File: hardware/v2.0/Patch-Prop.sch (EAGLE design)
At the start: 49 parts, among them IC1 TPS77033, IC2 XBEE, IC3 MMA8452Q, IC4 ATMEGA168, IC5 MCP1253, IC6 W2RV005RM, U2 MCP73831, X1 USBSMD

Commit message: Cleanup
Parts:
- added R10: 4.7k, rcl:R-US_R0603
- added R6: RLim, rcl:R-US_R0603
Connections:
- new net N$12: IC6.IN3, R9.1
- new net N$4: R6.2, T2.E
- new net N$7: IC6.IN1, R8.1
- new net N$9: IC6.IN2, R10.1
- net +3V3: no longer R8.2, R9.2
- net BLUE: now also R8.2; no longer IC6.IN1
- net GND: now also R6.1; no longer T2.E
- net GREEN: now also R10.2; no longer IC6.IN2
- net RED: now also R9.2; no longer IC6.IN3
- net SCL: no longer R9.1
- net SDA: no longer R8.1
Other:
- moved on the sheet: JP6, R8, R9, T2
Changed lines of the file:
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@@
 <part name="GND13" library="supply1" deviceset="GND" device=""/>
 <part name="SJ3" library="SparkFun" deviceset="SOLDERJUMPER" device="NO"/>
+<part name="R6" library="rcl" deviceset="R-US_" device="R0603" value="RLim"/>
 <part name="R8" library="rcl" deviceset="R-US_" device="R0603" value="4.7k"/>
 <part name="R9" library="rcl" deviceset="R-US_" device="R0603" value="4.7k"/>
-<part name="+3V14" library="supply1" deviceset="+3V3" device=""/>
-<part name="+3V15" library="supply1" deviceset="+3V3" device=""/>
+<part name="R10" library="rcl" deviceset="R-US_" device="R0603" value="4.7k"/>
 </parts>
 <sheets>
@@
 <instance part="SJ1" gate="1" x="424.18" y="350.52" rot="R180"/>
 <instance part="T1" gate="G$1" x="505.46" y="335.28" rot="R270"/>
-<instance part="T2" gate="G$1" x="86.36" y="104.14"/>
+<instance part="T2" gate="G$1" x="86.36" y="96.52"/>
 <instance part="GND11" gate="1" x="218.44" y="337.82"/>
 <instance part="LED1" gate="G$1" x="259.08" y="210.82"/>
@@
 <instance part="GND12" gate="1" x="259.08" y="200.66"/>
 <instance part="+3V10" gate="G$1" x="259.08" y="228.6"/>
-<instance part="GND10" gate="1" x="88.9" y="93.98"/>
+<instance part="GND10" gate="1" x="88.9" y="73.66"/>
 <instance part="U2" gate="G$1" x="114.3" y="335.28"/>
 <instance part="GND17" gate="1" x="101.6" y="312.42"/>
@@
 <instance part="P+3" gate="1" x="355.6" y="370.84"/>
 <instance part="+3V13" gate="G$1" x="269.24" y="370.84"/>
-<instance part="JP6" gate="G$1" x="78.74" y="71.12" rot="MR180"/>
-<instance part="SUPPLY6" gate="1" x="88.9" y="76.2"/>
+<instance part="JP6" gate="G$1" x="78.74" y="43.18" rot="MR180"/>
+<instance part="SUPPLY6" gate="1" x="88.9" y="48.26"/>
 <instance part="PROPINQUITY_V2" gate="G$1" x="0" y="0"/>
 <instance part="PROPINQUITY_V2" gate="G$2" x="452.12" y="0"/>
@@
 <instance part="GND13" gate="1" x="538.48" y="81.28"/>
 <instance part="SJ3" gate="1" x="213.36" y="231.14" rot="R180"/>
-<instance part="R8" gate="G$1" x="408.94" y="233.68" rot="R90"/>
-<instance part="R9" gate="G$1" x="401.32" y="233.68" rot="R90"/>
-<instance part="+3V14" gate="G$1" x="408.94" y="243.84"/>
-<instance part="+3V15" gate="G$1" x="401.32" y="243.84"/>
+<instance part="R6" gate="G$1" x="88.9" y="83.82" rot="R90"/>
+<instance part="R8" gate="G$1" x="467.36" y="99.06" rot="R180"/>
+<instance part="R9" gate="G$1" x="467.36" y="88.9" rot="R180"/>
+<instance part="R10" gate="G$1" x="467.36" y="93.98" rot="R180"/>
 </instances>
 <busses>
@@
 <wire x1="426.72" y1="335.28" x2="426.72" y2="337.82" width="0.1524" layer="91"/>
 <wire x1="426.72" y1="337.82" x2="431.8" y2="337.82" width="0.1524" layer="91"/>
-</segment>
-<segment>
-<pinref part="T2" gate="G$1" pin="E"/>
-<wire x1="88.9" y1="99.06" x2="88.9" y2="96.52" width="0.1524" layer="91"/>
-<pinref part="GND10" gate="1" pin="GND"/>
 </segment>
 <segment>
@@
 <wire x1="223.52" y1="195.58" x2="223.52" y2="193.04" width="0.1524" layer="91"/>
 </segment>
+<segment>
+<pinref part="R6" gate="G$1" pin="1"/>
+<pinref part="GND10" gate="1" pin="GND"/>
+<wire x1="88.9" y1="78.74" x2="88.9" y2="76.2" width="0.1524" layer="91"/>
+</segment>
 </net>
 <net name="+3V3" class="0">
@@
 </segment>
 <segment>
-<pinref part="+3V15" gate="G$1" pin="+3V3"/>
-<pinref part="R9" gate="G$1" pin="2"/>
-<wire x1="401.32" y1="241.3" x2="401.32" y2="238.76" width="0.1524" layer="91"/>
-</segment>
-<segment>
-<pinref part="+3V14" gate="G$1" pin="+3V3"/>
-<pinref part="R8" gate="G$1" pin="2"/>
-<wire x1="408.94" y1="241.3" x2="408.94" y2="238.76" width="0.1524" layer="91"/>
-</segment>
-<segment>
 <pinref part="ISP1" gate="A" pin="2"/>
 <pinref part="+3V7" gate="G$1" pin="+3V3"/>
@@
 <segment>
 <pinref part="SUPPLY6" gate="1" pin="V+"/>
-<wire x1="88.9" y1="71.12" x2="88.9" y2="73.66" width="0.1524" layer="91"/>
+<wire x1="88.9" y1="43.18" x2="88.9" y2="45.72" width="0.1524" layer="91"/>
 <pinref part="JP6" gate="G$1" pin="1"/>
-<wire x1="88.9" y1="71.12" x2="86.36" y2="71.12" width="0.1524" layer="91"/>
+<wire x1="88.9" y1="43.18" x2="86.36" y2="43.18" width="0.1524" layer="91"/>
 </segment>
 <segment>
@@
 <net name="RED" class="0">
 <segment>
-<pinref part="IC6" gate="G$1" pin="IN3"/>
-<wire x1="464.82" y1="88.9" x2="474.98" y2="88.9" width="0.1524" layer="91"/>
-<label x="464.82" y="88.9" size="1.27" layer="95" font="vector" ratio="15" rot="R180" xref="yes"/>
+<wire x1="459.74" y1="88.9" x2="462.28" y2="88.9" width="0.1524" layer="91"/>
+<label x="459.74" y="88.9" size="1.27" layer="95" font="vector" ratio="15" rot="R180" xref="yes"/>
+<pinref part="R9" gate="G$1" pin="2"/>
 </segment>
 <segment>
@@
 </segment>
 <segment>
-<pinref part="IC6" gate="G$1" pin="IN1"/>
-<wire x1="474.98" y1="99.06" x2="464.82" y2="99.06" width="0.1524" layer="91"/>
-<label x="464.82" y="99.06" size="1.27" layer="95" font="vector" ratio="15" rot="R180" xref="yes"/>
+<label x="459.74" y="99.06" size="1.27" layer="95" font="vector" ratio="15" rot="R180" xref="yes"/>
+<pinref part="R8" gate="G$1" pin="2"/>
+<wire x1="462.28" y1="99.06" x2="459.74" y2="99.06" width="0.1524" layer="91"/>
 </segment>
 </net>
@@
 <segment>
 <pinref part="T2" gate="G$1" pin="B"/>
-<wire x1="83.82" y1="104.14" x2="81.28" y2="104.14" width="0.1524" layer="91"/>
-<label x="81.28" y="104.14" size="1.27" layer="95" font="vector" ratio="15" rot="R180" xref="yes"/>
+<wire x1="83.82" y1="96.52" x2="81.28" y2="96.52" width="0.1524" layer="91"/>
+<label x="81.28" y="96.52" size="1.27" layer="95" font="vector" ratio="15" rot="R180" xref="yes"/>
 </segment>
 <segment>
@@
 <segment>
 <pinref part="T2" gate="G$1" pin="C"/>
-<wire x1="88.9" y1="109.22" x2="88.9" y2="111.76" width="0.1524" layer="91"/>
-<label x="88.9" y="111.76" size="1.27" layer="95" font="vector" ratio="15" rot="R90" xref="yes"/>
+<wire x1="88.9" y1="101.6" x2="88.9" y2="104.14" width="0.1524" layer="91"/>
+<label x="88.9" y="104.14" size="1.27" layer="95" font="vector" ratio="15" rot="R90" xref="yes"/>
 </segment>
 <segment>
 <pinref part="JP6" gate="G$1" pin="2"/>
-<wire x1="86.36" y1="68.58" x2="91.44" y2="68.58" width="0.1524" layer="91"/>
-<label x="91.44" y="68.58" size="1.27" layer="95" font="vector" ratio="15" xref="yes"/>
+<wire x1="86.36" y1="40.64" x2="91.44" y2="40.64" width="0.1524" layer="91"/>
+<label x="91.44" y="40.64" size="1.27" layer="95" font="vector" ratio="15" xref="yes"/>
 </segment>
 </net>
@@
 <net name="SCL" class="0">
 <segment>
-<wire x1="441.96" y1="220.98" x2="401.32" y2="220.98" width="0.1524" layer="91"/>
+<wire x1="441.96" y1="220.98" x2="393.7" y2="220.98" width="0.1524" layer="91"/>
 <label x="393.7" y="220.98" size="1.27" layer="95" font="vector" ratio="15" rot="R180" xref="yes"/>
 <pinref part="IC3" gate="G$1" pin="SCL"/>
-<pinref part="R9" gate="G$1" pin="1"/>
-<wire x1="401.32" y1="220.98" x2="393.7" y2="220.98" width="0.1524" layer="91"/>
-<wire x1="401.32" y1="228.6" x2="401.32" y2="220.98" width="0.1524" layer="91"/>
-<junction x="401.32" y="220.98"/>
 </segment>
 <segment>
@@
 <net name="SDA" class="0">
 <segment>
-<wire x1="441.96" y1="223.52" x2="408.94" y2="223.52" width="0.1524" layer="91"/>
+<wire x1="441.96" y1="223.52" x2="393.7" y2="223.52" width="0.1524" layer="91"/>
 <label x="393.7" y="223.52" size="1.27" layer="95" font="vector" ratio="15" rot="R180" xref="yes"/>
 <pinref part="IC3" gate="G$1" pin="SDA"/>
-<pinref part="R8" gate="G$1" pin="1"/>
-<wire x1="408.94" y1="223.52" x2="393.7" y2="223.52" width="0.1524" layer="91"/>
-<wire x1="408.94" y1="228.6" x2="408.94" y2="223.52" width="0.1524" layer="91"/>
-<junction x="408.94" y="223.52"/>
 </segment>
 <segment>
@@
 <net name="GREEN" class="0">
 <segment>
-<pinref part="IC6" gate="G$1" pin="IN2"/>
-<wire x1="474.98" y1="93.98" x2="464.82" y2="93.98" width="0.1524" layer="91"/>
-<label x="464.82" y="93.98" size="1.27" layer="95" font="vector" ratio="15" rot="R180" xref="yes"/>
+<label x="459.74" y="93.98" size="1.27" layer="95" font="vector" ratio="15" rot="R180" xref="yes"/>
+<pinref part="R10" gate="G$1" pin="2"/>
+<wire x1="459.74" y1="93.98" x2="462.28" y2="93.98" width="0.1524" layer="91"/>
 </segment>
 <segment>
@@
 </segment>
 </net>
+<net name="N$4" class="0">
+<segment>
+<pinref part="T2" gate="G$1" pin="E"/>
+<pinref part="R6" gate="G$1" pin="2"/>
+<wire x1="88.9" y1="91.44" x2="88.9" y2="88.9" width="0.1524" layer="91"/>
+</segment>
+</net>
+<net name="N$7" class="0">
+<segment>
+<pinref part="R8" gate="G$1" pin="1"/>
+<pinref part="IC6" gate="G$1" pin="IN1"/>
+<wire x1="472.44" y1="99.06" x2="474.98" y2="99.06" width="0.1524" layer="91"/>
+</segment>
+</net>
+<net name="N$9" class="0">
+<segment>
+<pinref part="R10" gate="G$1" pin="1"/>
+<pinref part="IC6" gate="G$1" pin="IN2"/>
+<wire x1="472.44" y1="93.98" x2="474.98" y2="93.98" width="0.1524" layer="91"/>
+</segment>
+</net>
+<net name="N$12" class="0">
+<segment>
+<pinref part="IC6" gate="G$1" pin="IN3"/>
+<pinref part="R9" gate="G$1" pin="1"/>
+<wire x1="474.98" y1="88.9" x2="472.44" y2="88.9" width="0.1524" layer="91"/>
+</segment>
+</net>

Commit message: Moved uC now routing LEDs
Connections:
- net GREEN: now also IC4.PD5(T1), R9.2; no longer IC4.PB1(OC1A), R10.2
- net GREEN_OUT: now also IC6.OUT3; no longer IC6.OUT2
- net RED: now also IC4.PB1(OC1A), R10.2; no longer IC4.PD5(T1), R9.2
- net RED_OUT: now also IC6.OUT2; no longer IC6.OUT3
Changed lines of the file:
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@@
 </segment>
 </net>
-<net name="RED" class="0">
+<net name="GREEN" class="0">
 <segment>
 <wire x1="459.74" y1="88.9" x2="462.28" y2="88.9" width="0.1524" layer="91"/>
@@
 </segment>
 </net>
-<net name="GREEN" class="0">
+<net name="RED" class="0">
 <segment>
 <label x="459.74" y="93.98" size="1.27" layer="95" font="vector" ratio="15" rot="R180" xref="yes"/>
@@
 </segment>
 <segment>
+<pinref part="IC6" gate="G$1" pin="OUT3"/>
+<wire x1="518.16" y1="83.82" x2="510.54" y2="83.82" width="0.1524" layer="91"/>
+<label x="518.16" y="83.82" size="1.27" layer="95" font="vector" ratio="15" xref="yes"/>
+</segment>
+</net>
+<net name="RED_OUT" class="0">
+<segment>
+<pinref part="LED3" gate="G$1" pin="RED_C"/>
+<wire x1="416.56" y1="111.76" x2="424.18" y2="111.76" width="0.1524" layer="91"/>
+<label x="424.18" y="111.76" size="1.27" layer="95" font="vector" ratio="15" xref="yes"/>
+</segment>
+<segment>
+<pinref part="LED4" gate="G$1" pin="RED_C"/>
+<wire x1="424.18" y1="86.36" x2="416.56" y2="86.36" width="0.1524" layer="91"/>
+<label x="424.18" y="86.36" size="1.27" layer="95" font="vector" ratio="15" xref="yes"/>
+</segment>
+<segment>
+<pinref part="LED5" gate="G$1" pin="RED_C"/>
+<wire x1="424.18" y1="63.5" x2="416.56" y2="63.5" width="0.1524" layer="91"/>
+<label x="424.18" y="63.5" size="1.27" layer="95" font="vector" ratio="15" xref="yes"/>
+</segment>
+<segment>
+<pinref part="LED6" gate="G$1" pin="RED_C"/>
+<wire x1="424.18" y1="40.64" x2="416.56" y2="40.64" width="0.1524" layer="91"/>
+<label x="424.18" y="40.64" size="1.27" layer="95" font="vector" ratio="15" xref="yes"/>
+</segment>
+<segment>
 <pinref part="IC6" gate="G$1" pin="OUT2"/>
 <wire x1="510.54" y1="88.9" x2="518.16" y2="88.9" width="0.1524" layer="91"/>
@@
 </segment>
 </net>
-<net name="RED_OUT" class="0">
-<segment>
-<pinref part="LED3" gate="G$1" pin="RED_C"/>
-<wire x1="416.56" y1="111.76" x2="424.18" y2="111.76" width="0.1524" layer="91"/>
-<label x="424.18" y="111.76" size="1.27" layer="95" font="vector" ratio="15" xref="yes"/>
-</segment>
-<segment>
-<pinref part="LED4" gate="G$1" pin="RED_C"/>
-<wire x1="424.18" y1="86.36" x2="416.56" y2="86.36" width="0.1524" layer="91"/>
-<label x="424.18" y="86.36" size="1.27" layer="95" font="vector" ratio="15" xref="yes"/>
-</segment>
-<segment>
-<pinref part="LED5" gate="G$1" pin="RED_C"/>
-<wire x1="424.18" y1="63.5" x2="416.56" y2="63.5" width="0.1524" layer="91"/>
-<label x="424.18" y="63.5" size="1.27" layer="95" font="vector" ratio="15" xref="yes"/>
-</segment>
-<segment>
-<pinref part="LED6" gate="G$1" pin="RED_C"/>
-<wire x1="424.18" y1="40.64" x2="416.56" y2="40.64" width="0.1524" layer="91"/>
-<label x="424.18" y="40.64" size="1.27" layer="95" font="vector" ratio="15" xref="yes"/>
-</segment>
-<segment>
-<pinref part="IC6" gate="G$1" pin="OUT3"/>
-<wire x1="518.16" y1="83.82" x2="510.54" y2="83.82" width="0.1524" layer="91"/>
-<label x="518.16" y="83.82" size="1.27" layer="95" font="vector" ratio="15" xref="yes"/>
-</segment>
-</net>

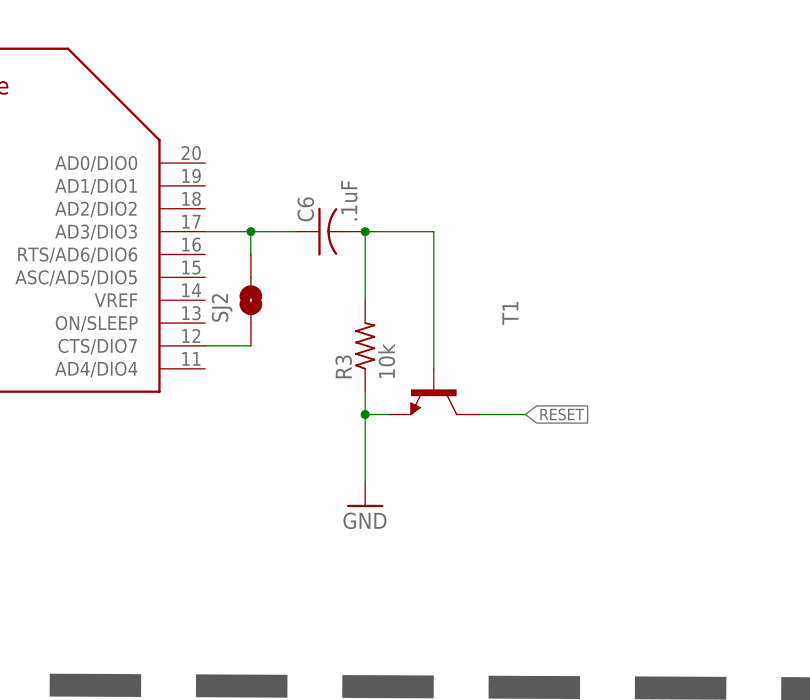
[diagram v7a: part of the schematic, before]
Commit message: Working on LED routing, remove Xbee reset
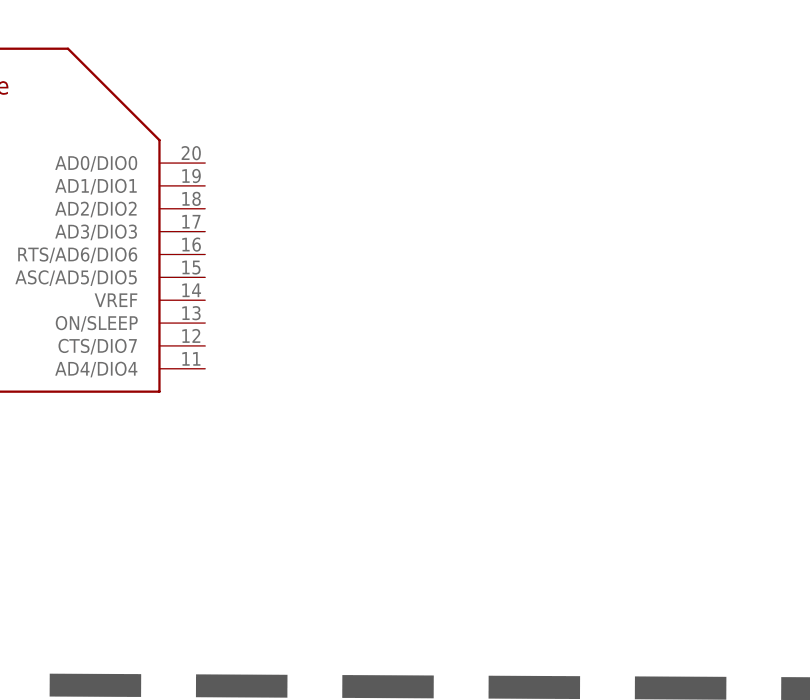
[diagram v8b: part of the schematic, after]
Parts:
- removed C6: .1uF, rcl:C-USC0603
- removed R3: 10k, rcl:R-US_R0603
- removed SJ2: SOLDERJUMPERNO, SparkFun:SOLDERJUMPERNO
- removed T1: (no value), transistor:-NPN-SOT23-EBC
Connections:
- removed net N$1: C6.1, IC2.AD3/DIO3, SJ2.2
- removed net N$18: IC2.CTS/DIO7, SJ2.1
- removed net N$2: C6.2, R3.2, T1.B
- net GND: no longer R3.1, T1.E
- net RESET: no longer T1.C
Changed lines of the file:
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@@
 <part name="C2" library="rcl" deviceset="C-US" device="C0603" value="4.7uF"/>
 <part name="C3" library="rcl" deviceset="C-US" device="C0603" value="1uF"/>
-<part name="R3" library="rcl" deviceset="R-US_" device="R0603" value="10k"/>
 <part name="+3V3" library="supply1" deviceset="+3V3" device=""/>
 <part name="SUPPLY1" library="supply2" deviceset="V+" device=""/>
@@
 <part name="+3V2" library="supply1" deviceset="+3V3" device=""/>
 <part name="GND1" library="supply1" deviceset="GND" device=""/>
-<part name="C6" library="rcl" deviceset="C-US" device="C0603" value=".1uF"/>
-<part name="GND2" library="supply1" deviceset="GND" device=""/>
 <part name="IC4" library="SparkFun" deviceset="ATMEGA168" device=""/>
 <part name="C13" library="rcl" deviceset="C-US" device="C0603" value="10uF"/>
@@
 <part name="LED5" library="adafruit" deviceset="RGBLED" device="5050"/>
 <part name="LED6" library="adafruit" deviceset="RGBLED" device="5050"/>
-<part name="SJ2" library="SparkFun" deviceset="SOLDERJUMPER" device="NO"/>
 <part name="SJ1" library="SparkFun" deviceset="SOLDERJUMPER" device="NO"/>
-<part name="T1" library="transistor" deviceset="*-NPN-" device="SOT23-EBC"/>
 <part name="T2" library="transistor" deviceset="*-NPN-" device="SOT23-EBC"/>
 <part name="GND11" library="supply1" deviceset="GND" device=""/>
@@
 <instance part="C2" gate="G$1" x="236.22" y="355.6"/>
 <instance part="C3" gate="G$1" x="190.5" y="353.06"/>
-<instance part="R3" gate="G$1" x="497.84" y="340.36" rot="R90"/>
 <instance part="+3V3" gate="G$1" x="236.22" y="368.3"/>
 <instance part="SUPPLY1" gate="1" x="190.5" y="368.3"/>
@@
 <instance part="+3V2" gate="G$1" x="421.64" y="368.3"/>
 <instance part="GND1" gate="1" x="426.72" y="332.74"/>
-<instance part="C6" gate="G$1" x="492.76" y="353.06" rot="R90"/>
-<instance part="GND2" gate="1" x="497.84" y="322.58"/>
 <instance part="IC4" gate="G$1" x="259.08" y="78.74"/>
 <instance part="C13" gate="G$1" x="205.74" y="76.2"/>
@@
 <instance part="LED5" gate="G$1" x="411.48" y="68.58"/>
 <instance part="LED6" gate="G$1" x="411.48" y="45.72"/>
-<instance part="SJ2" gate="1" x="485.14" y="345.44" rot="R90"/>
 <instance part="SJ1" gate="1" x="424.18" y="350.52" rot="R180"/>
-<instance part="T1" gate="G$1" x="505.46" y="335.28" rot="R270"/>
 <instance part="T2" gate="G$1" x="86.36" y="96.52"/>
 <instance part="GND11" gate="1" x="218.44" y="337.82"/>
@@
 <net name="GND" class="0">
 <segment>
-<pinref part="R3" gate="G$1" pin="1"/>
-<pinref part="GND2" gate="1" pin="GND"/>
-<wire x1="497.84" y1="335.28" x2="497.84" y2="332.74" width="0.1524" layer="91"/>
-<wire x1="497.84" y1="332.74" x2="497.84" y2="325.12" width="0.1524" layer="91"/>
-<wire x1="500.38" y1="332.74" x2="497.84" y2="332.74" width="0.1524" layer="91"/>
-<junction x="497.84" y="332.74"/>
-<pinref part="T1" gate="G$1" pin="E"/>
-</segment>
-<segment>
 <pinref part="IC4" gate="G$1" pin="GND@1"/>
 <wire x1="236.22" y1="50.8" x2="228.6" y2="50.8" width="0.1524" layer="91"/>
@@
 </segment>
 </net>
-<net name="N$1" class="0">
-<segment>
-<pinref part="IC2" gate="G$1" pin="AD3/DIO3"/>
-<pinref part="C6" gate="G$1" pin="1"/>
-<wire x1="490.22" y1="353.06" x2="485.14" y2="353.06" width="0.1524" layer="91"/>
-<pinref part="SJ2" gate="1" pin="2"/>
-<wire x1="485.14" y1="353.06" x2="480.06" y2="353.06" width="0.1524" layer="91"/>
-<wire x1="485.14" y1="350.52" x2="485.14" y2="353.06" width="0.1524" layer="91"/>
-<junction x="485.14" y="353.06"/>
-</segment>
-</net>
-<net name="N$2" class="0">
-<segment>
-<pinref part="C6" gate="G$1" pin="2"/>
-<pinref part="R3" gate="G$1" pin="2"/>
-<wire x1="497.84" y1="345.44" x2="497.84" y2="353.06" width="0.1524" layer="91"/>
-<wire x1="497.84" y1="353.06" x2="505.46" y2="353.06" width="0.1524" layer="91"/>
-<junction x="497.84" y="353.06"/>
-<wire x1="505.46" y1="353.06" x2="505.46" y2="337.82" width="0.1524" layer="91"/>
-<pinref part="T1" gate="G$1" pin="B"/>
-</segment>
-</net>
 <net name="RESET" class="0">
-<segment>
-<wire x1="510.54" y1="332.74" x2="515.62" y2="332.74" width="0.1524" layer="91"/>
-<label x="515.62" y="332.74" size="1.27" layer="95" font="vector" ratio="15" xref="yes"/>
-<pinref part="T1" gate="G$1" pin="C"/>
-</segment>
 <segment>
 <pinref part="IC4" gate="G$1" pin="PC6(/RESET)"/>
@@
 </segment>
 </net>
-<net name="N$18" class="0">
-<segment>
-<pinref part="IC2" gate="G$1" pin="CTS/DIO7"/>
-<pinref part="SJ2" gate="1" pin="1"/>
-<wire x1="480.06" y1="340.36" x2="485.14" y2="340.36" width="0.1524" layer="91"/>
-</segment>
-</net>
